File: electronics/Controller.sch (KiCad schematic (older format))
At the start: 18 parts, among them IC1 Teensy++2.0, J1 Input 5v

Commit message: Num&Caps control with LEDs
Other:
- note added: "Led\nPWM"
- note removed: "PWM"
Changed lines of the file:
@@
 Wire Notes Line
 	5350 3050 4800 3050
-Text Notes 5200 3050 0    35   ~ 0
-PWM
+Text Notes 5350 3050 2    35   ~ 0
+Led\nPWM
 $EndSCHEMATC

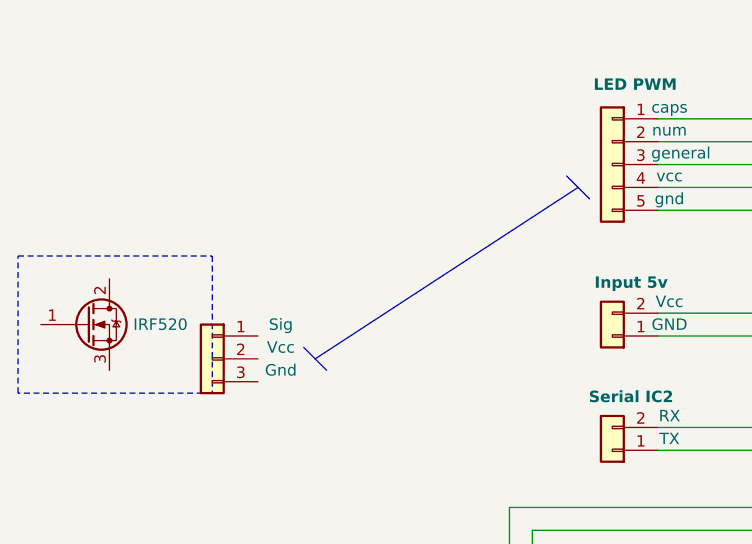
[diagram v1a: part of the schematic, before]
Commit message: Led backlight schematics
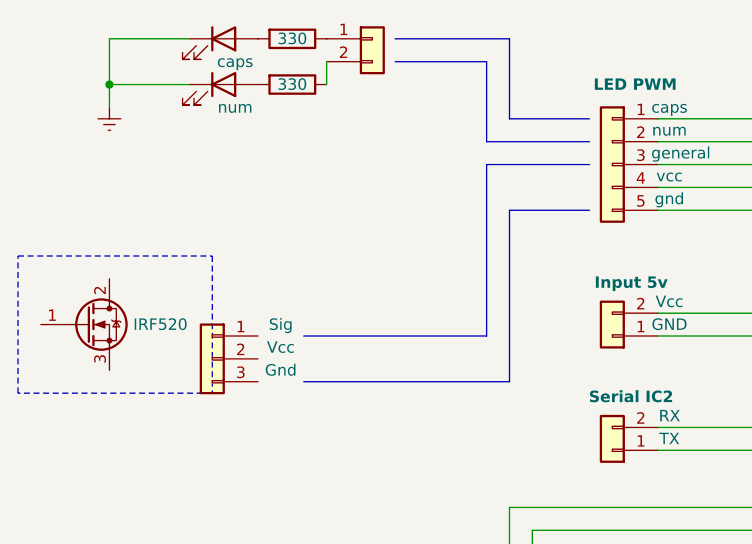
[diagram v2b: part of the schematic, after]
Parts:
- added J?: Serial IC2, symbol Connector_Generic:Conn_01x02
- added R? (x2): 330, symbol Device:R
- added caps, num: LED, symbol Device:LED
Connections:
- new net: J?.2 (Pin_2), R?.1
- new net: R?.2, num.2 (A)
- new net: J?.1 (Pin_1), R?.1
- new net: R?.2, caps.2 (A)
- new net GNDREF: caps.1 (K), num.1 (K)
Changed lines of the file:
@@
 	-1   0    0    -1
 $EndComp
-Wire Bus Line
-	1850 2300 3000 1550
-Entry Bus Bus
-	1800 2250 1900 2350
-Entry Bus Bus
-	2950 1500 3050 1600
 Wire Wire Line
 	4600 2800 4650 2800
@@
 Text Notes 5350 3050 2    35   ~ 0
 Led\nPWM
+$Comp
+L Device:R R?
+U 1 1 5F335569
+P 1750 1100
+F 0 "R?" V 1543 1100 50  0001 C CNN
+F 1 "330" V 1750 1100 50  0000 C CNN
+F 2 "" V 1680 1100 50  0001 C CNN
+F 3 "~" H 1750 1100 50  0001 C CNN
+	1    1750 1100
+	0    1    1    0
+$EndComp
+$Comp
+L Device:LED num
+U 1 1 5F3383DE
+P 1450 1100
+F 0 "num" H 1500 1000 50  0000 C CNN
+F 1 "LED" H 1443 1226 50  0001 C CNN
+F 2 "" H 1450 1100 50  0001 C CNN
+F 3 "~" H 1450 1100 50  0001 C CNN
+	1    1450 1100
+	1    0    0    -1
+$EndComp
+$Comp
+L Device:R R?
+U 1 1 5F3485EF
+P 1750 900
+F 0 "R?" V 1543 900 50  0001 C CNN
+F 1 "330" V 1750 900 50  0000 C CNN
+F 2 "" V 1680 900 50  0001 C CNN
+F 3 "~" H 1750 900 50  0001 C CNN
+	1    1750 900
+	0    1    1    0
+$EndComp
+$Comp
+L Device:LED caps
+U 1 1 5F356812
+P 1450 900
+F 0 "caps" H 1500 800 50  0000 C CNN
+F 1 "LED" H 1443 1026 50  0001 C CNN
+F 2 "" H 1450 900 50  0001 C CNN
+F 3 "~" H 1450 900 50  0001 C CNN
+	1    1450 900
+	1    0    0    -1
+$EndComp
+$Comp
+L power:GNDREF #PWR?
+U 1 1 5F369D14
+P 950 1200
+F 0 "#PWR?" H 950 950 50  0001 C CNN
+F 1 "GNDREF" H 955 1027 50  0001 C CNN
+F 2 "" H 950 1200 50  0001 C CNN
+F 3 "" H 950 1200 50  0001 C CNN
+	1    950  1200
+	1    0    0    -1
+$EndComp
+Wire Wire Line
+	950  1100 1300 1100
+Wire Wire Line
+	950  1100 950  900
+Wire Wire Line
+	950  900  1300 900
+Connection ~ 950  1100
+$Comp
+L Connector_Generic:Conn_01x02 J?
+U 1 1 5F373DAA
+P 2100 900
+F 0 "J?" H 2018 575 50  0001 C CNN
+F 1 "Serial IC2" H 2018 666 50  0001 C CNN
+F 2 "" H 2100 900 50  0001 C CNN
+F 3 "~" H 2100 900 50  0001 C CNN
+	1    2100 900
+	1    0    0    -1
+$EndComp
+Wire Wire Line
+	1900 1000 1900 1100
+Wire Wire Line
+	950  1100 950  1200
+Wire Bus Line
+	2200 1000 2600 1000
+Wire Bus Line
+	2600 1000 2600 1350
+Wire Bus Line
+	2600 1350 3050 1350
+Wire Bus Line
+	3050 1450 2600 1450
+Wire Bus Line
+	2600 1450 2600 2200
+Wire Bus Line
+	2600 2200 1800 2200
+Wire Bus Line
+	1800 2400 2700 2400
+Wire Bus Line
+	2700 2400 2700 1650
+Wire Bus Line
+	2700 1650 3050 1650
+Wire Bus Line
+	2200 900  2700 900
+Wire Bus Line
+	2700 900  2700 1250
+Wire Bus Line
+	2700 1250 3050 1250
 $EndSCHEMATC
